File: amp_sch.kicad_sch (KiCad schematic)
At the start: 6 parts, among them IC1 AD7730, U1 74LVC125APW,118

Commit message: Footprint assignment
Footprints yet to be assigned:
-U1: 74LVC125APW
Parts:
- C1, C2, C3: footprint Capacitor_SMD:C_0201_0603Metric -> Capacitor_SMD:C_0603_1608Metric
- IC1: footprint (none) -> Package_SO:SOIC-14_3.9x8.7mm_P1.27mm
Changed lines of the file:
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@@
       (effects (font (size 1.27 1.27)) (justify right))
     )
-    (property "Footprint" "Capacitor_SMD:C_0201_0603Metric" (id 2) (at 240.665 85.09 0)
+    (property "Footprint" "Capacitor_SMD:C_0603_1608Metric" (id 2) (at 240.665 85.09 0)
       (effects (font (size 1.27 1.27)) hide)
     )
@@
       (effects (font (size 1.27 1.27)) (justify right))
     )
-    (property "Footprint" "Capacitor_SMD:C_0201_0603Metric" (id 2) (at 163.195 85.09 0)
+    (property "Footprint" "Capacitor_SMD:C_0603_1608Metric" (id 2) (at 163.195 85.09 0)
       (effects (font (size 1.27 1.27)) hide)
     )
@@
       (effects (font (size 1.27 1.27)) (justify right))
     )
-    (property "Footprint" "Capacitor_SMD:C_0201_0603Metric" (id 2) (at 168.275 85.09 0)
+    (property "Footprint" "Capacitor_SMD:C_0603_1608Metric" (id 2) (at 168.275 85.09 0)
       (effects (font (size 1.27 1.27)) hide)
     )
@@
     (property "Reference" "IC1" (id 0) (at 199.39 74.93 0))
     (property "Value" "AD7730" (id 1) (at 199.39 77.47 0))
-    (property "Footprint" "" (id 2) (at 199.39 107.95 0)
+    (property "Footprint" "Package_SO:SOIC-14_3.9x8.7mm_P1.27mm" (id 2) (at 199.39 107.95 0)
       (effects (font (size 1.27 1.27)) hide)
     )

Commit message: FIxed J1-Headers conflict
Added a layout
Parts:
- U1: footprint SOP65P640X110-14N -> (none)
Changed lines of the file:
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@@
     (property "Reference" "U1" (id 0) (at 102.87 84.455 0))
     (property "Value" "74LVC125APW,118" (id 1) (at 102.87 86.995 0))
-    (property "Footprint" "SOP65P640X110-14N" (id 2) (at 102.87 107.315 0)
+    (property "Footprint" "" (id 2) (at 102.87 107.315 0)
       (effects (font (size 1.27 1.27)) (justify left bottom) hide)
     )

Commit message: Component placement
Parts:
- U1: footprint (none) -> 74LVC125APW_118:SOP65P640X110-14N
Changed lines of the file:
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@@
     (property "Reference" "U1" (id 0) (at 102.87 84.455 0))
     (property "Value" "74LVC125APW,118" (id 1) (at 102.87 86.995 0))
-    (property "Footprint" "" (id 2) (at 102.87 107.315 0)
+    (property "Footprint" "74LVC125APW_118:SOP65P640X110-14N" (id 2) (at 102.87 107.315 0)
       (effects (font (size 1.27 1.27)) (justify left bottom) hide)
     )

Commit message: Reassigned pins to match placement
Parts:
- IC1: footprint Package_SO:SOIC-14_3.9x8.7mm_P1.27mm -> Package_SO:TSSOP-24_4.4x7.8mm_P0.65mm
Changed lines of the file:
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@@
     (property "Reference" "IC1" (id 0) (at 199.39 74.93 0))
     (property "Value" "AD7730" (id 1) (at 199.39 77.47 0))
-    (property "Footprint" "Package_SO:SOIC-14_3.9x8.7mm_P1.27mm" (id 2) (at 199.39 107.95 0)
+    (property "Footprint" "Package_SO:TSSOP-24_4.4x7.8mm_P0.65mm" (id 2) (at 199.39 107.95 0)
       (effects (font (size 1.27 1.27)) hide)
     )

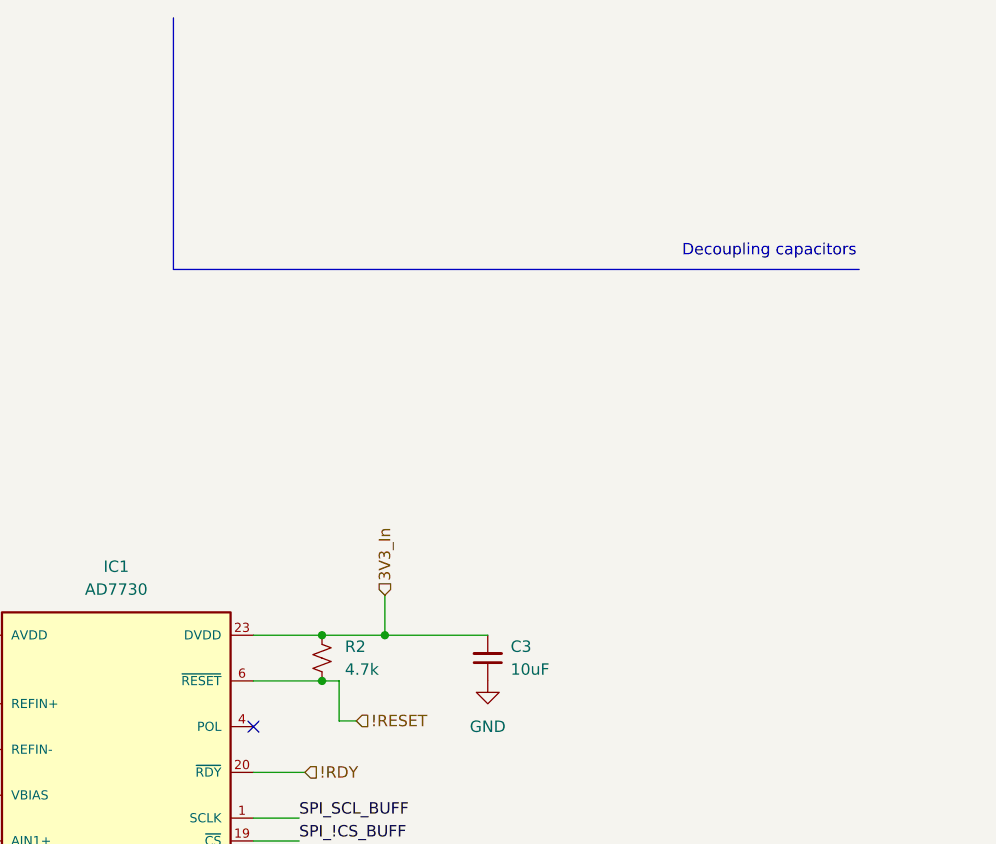
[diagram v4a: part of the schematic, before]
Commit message: placement refinement and indicator LEDs for relays
-Crude wiring
-Fixed values
-Indicator LEDs for  relays
-Added test points
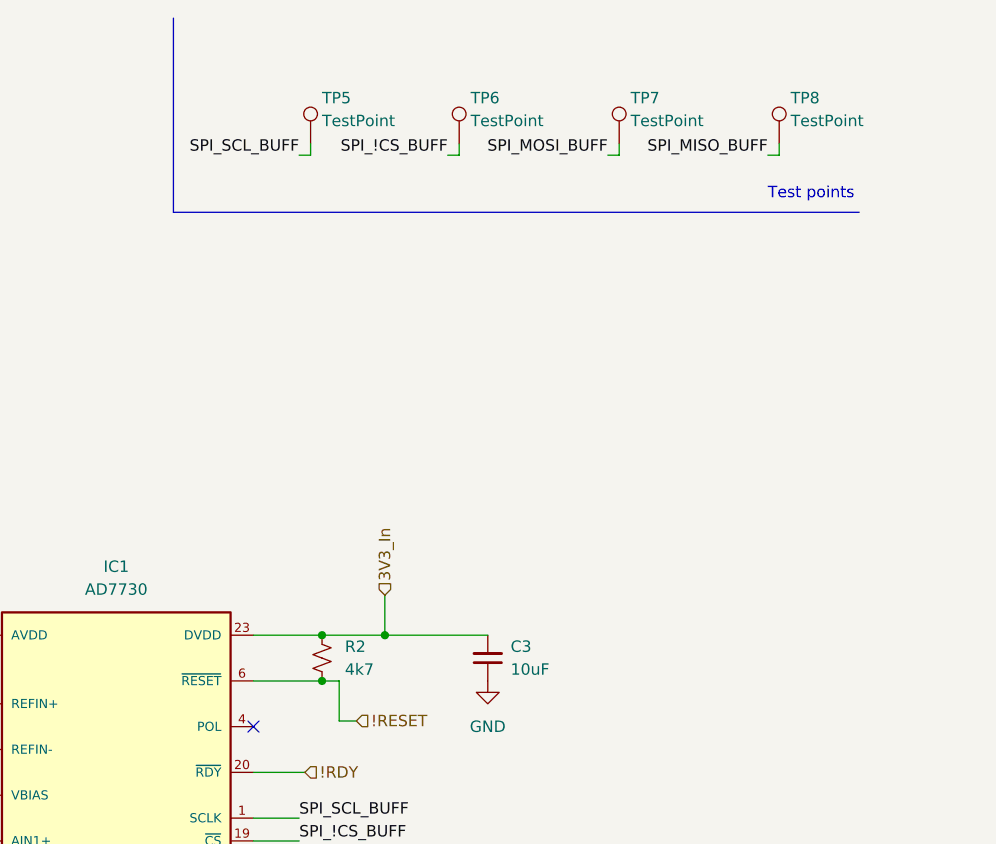
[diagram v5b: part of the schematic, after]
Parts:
- added TP5, TP6, TP7, TP8: TestPoint, TestPoint:TestPoint_Pad_D1.5mm, symbol Connector:TestPoint
- R2: value 4.7k -> 4k7
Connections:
- net SPI_!CS_BUFF: now also TP6.1
- net SPI_MISO_BUFF: now also TP8.1
- net SPI_MOSI_BUFF: now also TP7.1
- net SPI_SCL_BUFF: now also TP5.1
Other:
- note added: "Test points"
- note removed: "Decoupling capacitors"
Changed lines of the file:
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@@
+    (stroke (width 0) (type default) (color 0 0 0 0))
+  )
+  (wire (pts (xy 255.27 29.21) (xy 254 29.21))
     (stroke (width 0) (type default) (color 0 0 0 0))
   )
@@
     (stroke (width 0) (type default) (color 0 0 0 0))
   )
-  (polyline (pts (xy 281.94 41.91) (xy 205.74 41.91))
+  (polyline (pts (xy 281.94 35.56) (xy 205.74 35.56))
     (stroke (width 0) (type default) (color 0 0 0 0))
   )
@@
     (stroke (width 0) (type default) (color 0 0 0 0))
   )
+  (wire (pts (xy 255.27 27.94) (xy 255.27 29.21))
+    (stroke (width 0) (type default) (color 0 0 0 0))
+  )
+  (wire (pts (xy 237.49 27.94) (xy 237.49 29.21))
+    (stroke (width 0) (type default) (color 0 0 0 0))
+  )
   (wire (pts (xy 165.735 87.63) (xy 165.735 90.17))
     (stroke (width 0) (type default) (color 0 0 0 0))
@@
     (stroke (width 0) (type default) (color 0 0 0 0))
   )
-  (polyline (pts (xy 205.74 13.97) (xy 205.74 41.91))
+  (polyline (pts (xy 205.74 13.97) (xy 205.74 35.56))
     (stroke (width 0) (type default) (color 0 0 0 0))
   )
@@
     (stroke (width 0) (type default) (color 0 0 0 0))
   )
+  (wire (pts (xy 220.98 27.94) (xy 220.98 29.21))
+    (stroke (width 0) (type default) (color 0 0 0 0))
+  )
   (wire (pts (xy 214.63 107.95) (xy 219.71 107.95))
     (stroke (width 0) (type default) (color 0 0 0 0))
@@
     (stroke (width 0) (type default) (color 0 0 0 0))
   )
+  (wire (pts (xy 237.49 29.21) (xy 236.22 29.21))
+    (stroke (width 0) (type default) (color 0 0 0 0))
+  )
+  (wire (pts (xy 220.98 29.21) (xy 219.71 29.21))
+    (stroke (width 0) (type default) (color 0 0 0 0))
+  )
   (wire (pts (xy 177.8 110.49) (xy 184.15 110.49))
     (stroke (width 0) (type default) (color 0 0 0 0))
   )
+  (wire (pts (xy 273.05 29.21) (xy 271.78 29.21))
+    (stroke (width 0) (type default) (color 0 0 0 0))
+  )
   (wire (pts (xy 173.99 82.55) (xy 184.15 82.55))
+    (stroke (width 0) (type default) (color 0 0 0 0))
+  )
+  (wire (pts (xy 273.05 27.94) (xy 273.05 29.21))
     (stroke (width 0) (type default) (color 0 0 0 0))
   )
@@
     (effects (font (size 1.27 1.27)) (justify left bottom))
   )
-  (text "Decoupling capacitors" (at 262.255 40.64 0)
-    (effects (font (size 1.27 1.27)) (justify left bottom))
+  (text "Test points" (at 271.78 34.29 0)
+    (effects (font (size 1.27 1.27)) (justify left bottom))
+  )
+  (label "SPI_SCL_BUFF" (at 219.71 29.21 180)
+    (effects (font (size 1.27 1.27)) (justify right bottom))
   )
   (label "SPI_MISO_BUFF" (at 69.215 120.015 0)
     (effects (font (size 1.27 1.27)) (justify left bottom))
   )
+  (label "SPI_MOSI_BUFF" (at 254 29.21 180)
+    (effects (font (size 1.27 1.27)) (justify right bottom))
+  )
   (label "SPI_MISO_BUFF" (at 219.71 110.49 0)
     (effects (font (size 1.27 1.27)) (justify left bottom))
@@
     (effects (font (size 1.27 1.27)) (justify left bottom))
   )
+  (label "SPI_!CS_BUFF" (at 236.22 29.21 180)
+    (effects (font (size 1.27 1.27)) (justify right bottom))
+  )
+  (label "SPI_MISO_BUFF" (at 271.78 29.21 180)
+    (effects (font (size 1.27 1.27)) (justify right bottom))
+  )
   (hierarchical_label "AIN1-" (shape input) (at 177.8 110.49 180)
     (effects (font (size 1.27 1.27)) (justify right))
@@
     (pin "1")
     (pin "2")
+  )
+  (symbol (lib_id "Connector:TestPoint") (at 273.05 27.94 0) (unit 1)
+    (in_bom yes) (on_board yes)
+    (property "Reference" "TP8" (id 0) (at 274.32 22.86 0)
+      (effects (font (size 1.27 1.27)) (justify left))
+    )
+    (property "Value" "TestPoint" (id 1) (at 274.32 25.4 0)
+      (effects (font (size 1.27 1.27)) (justify left))
+    )
+    (property "Footprint" "TestPoint:TestPoint_Pad_D1.5mm" (id 2) (at 278.13 27.94 0)
+      (effects (font (size 1.27 1.27)) hide)
+    )
+    (property "Datasheet" "~" (id 3) (at 278.13 27.94 0)
+      (effects (font (size 1.27 1.27)) hide)
+    )
+    (pin "1")
   )
   (symbol (lib_id "power:GND") (at 85.09 125.095 0) (unit 1)
@@
     (pin "2")
   )
+  (symbol (lib_id "Connector:TestPoint") (at 237.49 27.94 0) (unit 1)
+    (in_bom yes) (on_board yes)
+    (property "Reference" "TP6" (id 0) (at 238.76 22.86 0)
+      (effects (font (size 1.27 1.27)) (justify left))
+    )
+    (property "Value" "TestPoint" (id 1) (at 238.76 25.4 0)
+      (effects (font (size 1.27 1.27)) (justify left))
+    )
+    (property "Footprint" "TestPoint:TestPoint_Pad_D1.5mm" (id 2) (at 242.57 27.94 0)
+      (effects (font (size 1.27 1.27)) hide)
+    )
+    (property "Datasheet" "~" (id 3) (at 242.57 27.94 0)
+      (effects (font (size 1.27 1.27)) hide)
+    )
+    (pin "1")
+  )
   (symbol (lib_id "Device:R_Small_US") (at 222.25 85.09 180) (unit 1)
     (in_bom yes) (on_board yes) (fields_autoplaced)
@@
       (effects (font (size 1.27 1.27)) (justify right))
     )
-    (property "Value" "4.7k" (id 1) (at 224.79 86.3599 0)
+    (property "Value" "4k7" (id 1) (at 224.79 86.3599 0)
       (effects (font (size 1.27 1.27)) (justify right))
     )
@@
       (effects (font (size 1.27 1.27)) hide)
     )
+    (pin "1")
+  )
+  (symbol (lib_id "Connector:TestPoint") (at 255.27 27.94 0) (unit 1)
+    (in_bom yes) (on_board yes)
+    (property "Reference" "TP7" (id 0) (at 256.54 22.86 0)
+      (effects (font (size 1.27 1.27)) (justify left))
+    )
+    (property "Value" "TestPoint" (id 1) (at 256.54 25.4 0)
+      (effects (font (size 1.27 1.27)) (justify left))
+    )
+    (property "Footprint" "TestPoint:TestPoint_Pad_D1.5mm" (id 2) (at 260.35 27.94 0)
+      (effects (font (size 1.27 1.27)) hide)
+    )
+    (property "Datasheet" "~" (id 3) (at 260.35 27.94 0)
+      (effects (font (size 1.27 1.27)) hide)
+    )
+    (pin "1")
+  )
+  (symbol (lib_id "Connector:TestPoint") (at 220.98 27.94 0) (unit 1)
+    (in_bom yes) (on_board yes)
+    (property "Reference" "TP5" (id 0) (at 222.25 22.86 0)
+      (effects (font (size 1.27 1.27)) (justify left))
+    )
+    (property "Value" "TestPoint" (id 1) (at 222.25 25.4 0)
+      (effects (font (size 1.27 1.27)) (justify left))
+    )
+    (property "Footprint" "TestPoint:TestPoint_Pad_D1.5mm" (id 2) (at 226.06 27.94 0)
+      (effects (font (size 1.27 1.27)) hide)
+    )
+    (property "Datasheet" "~" (id 3) (at 226.06 27.94 0)
+      (effects (font (size 1.27 1.27)) hide)
+    )

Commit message: Review and fixes on schematic and pcb.
-Updated Relay LED values.
-Fixed !RDY and R1 pin conflict on GPIO26.
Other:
- note added: "all spi done via buffer"
- note removed: "CS pin is active low. Allows spi cmmunication when active"
- note removed: "OE, active low. Sets buffers to high impedance at high"
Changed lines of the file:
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@@
     (stroke (width 0) (type default) (color 0 0 0 0))
   )
-  (text "CS pin is active low. Allows spi cmmunication when active"
-    (at 224.79 118.745 0)
+  (text "all spi done via buffer " (at 55.88 123.19 0)
     (effects (font (size 1.27 1.27)) (justify left bottom))
   )
-  (text "OE, active low. Sets buffers to\nhigh impedance at high"
-    (at 52.705 105.41 0)
+  (text "all spi done via buffer " (at 121.285 106.045 0)
     (effects (font (size 1.27 1.27)) (justify left bottom))
   )

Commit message: Improvements made to the info in the schematic excel sheet and made the files necessary for production
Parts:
- C1, C2, C3: Extended (none) -> 0; LCSC (none) -> C96446; Populate (none) -> 1; Price (none) -> 0.024
- IC1, TP5, TP6, TP7, TP8: Populate (none) -> 0
- R2: Extended (none) -> 0; LCSC (none) -> C25900; Populate (none) -> 1
- U1: Extended (none) -> 1; LCSC (none) -> C6059; Populate (none) -> 1; Price (none) -> 0.5
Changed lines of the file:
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@@
+      (effects (font (size 1.27 1.27)) hide)
+    )
+    (property "Extended" "0" (id 4) (at 240.665 85.09 0)
+      (effects (font (size 1.27 1.27)) hide)
+    )
+    (property "LCSC" "C96446" (id 5) (at 240.665 85.09 0)
+      (effects (font (size 1.27 1.27)) hide)
+    )
+    (property "Populate" "1" (id 6) (at 240.665 85.09 0)
+      (effects (font (size 1.27 1.27)) hide)
+    )
+    (property "Price" "0.024" (id 7) (at 240.665 85.09 0)
       (effects (font (size 1.27 1.27)) hide)
     )
@@
     )
     (property "Datasheet" "~" (id 3) (at 278.13 27.94 0)
+      (effects (font (size 1.27 1.27)) hide)
+    )
+    (property "Populate" "0" (id 4) (at 273.05 27.94 0)
       (effects (font (size 1.27 1.27)) hide)
     )
@@
       (effects (font (size 1.27 1.27)) hide)
     )
+    (property "Extended" "0" (id 4) (at 163.195 85.09 0)
+      (effects (font (size 1.27 1.27)) hide)
+    )
+    (property "LCSC" "C96446" (id 5) (at 163.195 85.09 0)
+      (effects (font (size 1.27 1.27)) hide)
+    )
+    (property "Populate" "1" (id 6) (at 163.195 85.09 0)
+      (effects (font (size 1.27 1.27)) hide)
+    )
+    (property "Price" "0.024" (id 7) (at 163.195 85.09 0)
+      (effects (font (size 1.27 1.27)) hide)
+    )
     (pin "1")
     (pin "2")
@@
       (effects (font (size 1.27 1.27)) hide)
     )
+    (property "Populate" "0" (id 4) (at 237.49 27.94 0)
+      (effects (font (size 1.27 1.27)) hide)
+    )
     (pin "1")
   )
@@
     )
     (property "Datasheet" "~" (id 3) (at 222.25 85.09 0)
+      (effects (font (size 1.27 1.27)) hide)
+    )
+    (property "Populate" "1" (id 4) (at 222.25 85.09 0)
+      (effects (font (size 1.27 1.27)) hide)
+    )
+    (property "Extended" "0" (id 5) (at 222.25 85.09 0)
+      (effects (font (size 1.27 1.27)) hide)
+    )
+    (property "LCSC" "C25900" (id 6) (at 222.25 85.09 0)
       (effects (font (size 1.27 1.27)) hide)
     )
@@
       (effects (font (size 1.27 1.27)) hide)
     )
+    (property "Extended" "0" (id 4) (at 168.275 85.09 0)
+      (effects (font (size 1.27 1.27)) hide)
+    )
+    (property "LCSC" "C96446" (id 5) (at 168.275 85.09 0)
+      (effects (font (size 1.27 1.27)) hide)
+    )
+    (property "Populate" "1" (id 6) (at 168.275 85.09 0)
+      (effects (font (size 1.27 1.27)) hide)
+    )
+    (property "Price" "0.024" (id 7) (at 168.275 85.09 0)
+      (effects (font (size 1.27 1.27)) hide)
+    )
     (pin "1")
     (pin "2")
@@
       (effects (font (size 1.27 1.27)) hide)
     )
+    (property "Populate" "0" (id 4) (at 255.27 27.94 0)
+      (effects (font (size 1.27 1.27)) hide)
+    )
     (pin "1")
   )
@@
     )
     (property "Datasheet" "~" (id 3) (at 226.06 27.94 0)
+      (effects (font (size 1.27 1.27)) hide)
+    )
+    (property "Populate" "0" (id 4) (at 220.98 27.94 0)
       (effects (font (size 1.27 1.27)) hide)
     )
@@
     (property "MPN" "74LVC125APW,118" (id 8) (at 102.87 107.315 0)
       (effects (font (size 1.27 1.27)) (justify left bottom) hide)
+    )
+    (property "Extended" "1" (id 9) (at 102.87 107.315 0)
+      (effects (font (size 1.27 1.27)) hide)
+    )
+    (property "LCSC" "C6059" (id 10) (at 102.87 107.315 0)
+      (effects (font (size 1.27 1.27)) hide)
+    )
+    (property "Populate" "1" (id 11) (at 102.87 107.315 0)
+      (effects (font (size 1.27 1.27)) hide)
+    )
+    (property "Price" "0.5" (id 12) (at 102.87 107.315 0)
+      (effects (font (size 1.27 1.27)) hide)
     )
     (pin "1")
@@
       (effects (font (size 1.27 1.27)) (justify left bottom) hide)
     )
-    (pin "1")
+    (property "Populate" "0" (id 4) (at 199.39 107.95 0)
+      (effects (font (size 1.27 1.27)) hide)
+    )
+    (pin "1")
